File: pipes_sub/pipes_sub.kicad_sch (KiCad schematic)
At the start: 28 parts, among them J1 2x8 Header, J2 2x5 Header, J4 2x5 Header, U2 TL072CP

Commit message: Changes labels: VCO to SIG
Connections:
- net VCO renamed SIG
- net VCO1 renamed SIG1
- net VCO2 renamed SIG2
- net VCO3 renamed SIG3
- net VCO4 renamed SIG4
- net VCO5 renamed SIG5
- net VCO6 renamed SIG6
- net VCO7 renamed SIG7
- net VCO8 renamed SIG8
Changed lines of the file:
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@@
     )
   )
-  (global_label "VCO8" (shape input) (at 195.326 76.2 180) (fields_autoplaced)
+  (global_label "SIG8" (shape input) (at 195.326 76.2 180) (fields_autoplaced)
     (effects (font (size 1.27 1.27)) (justify right))
     (property "Intersheet References" "${INTERSHEET_REFS}" (id 0) (at 188.0143 76.1206 0)
@@
     )
   )
-  (global_label "VCO4" (shape input) (at 195.326 45.72 180) (fields_autoplaced)
+  (global_label "SIG4" (shape input) (at 195.326 45.72 180) (fields_autoplaced)
     (effects (font (size 1.27 1.27)) (justify right))
     (property "Intersheet References" "${INTERSHEET_REFS}" (id 0) (at 188.0143 45.6406 0)
@@
     )
   )
-  (global_label "VCO7" (shape input) (at 195.326 68.58 180) (fields_autoplaced)
+  (global_label "SIG7" (shape input) (at 195.326 68.58 180) (fields_autoplaced)
     (effects (font (size 1.27 1.27)) (justify right))
     (property "Intersheet References" "${INTERSHEET_REFS}" (id 0) (at 188.0143 68.5006 0)
@@
     )
   )
-  (global_label "VCO6" (shape input) (at 195.326 60.96 180) (fields_autoplaced)
+  (global_label "SIG6" (shape input) (at 195.326 60.96 180) (fields_autoplaced)
     (effects (font (size 1.27 1.27)) (justify right))
     (property "Intersheet References" "${INTERSHEET_REFS}" (id 0) (at 188.0143 60.8806 0)
@@
     )
   )
-  (global_label "VCO1" (shape input) (at 195.326 22.86 180) (fields_autoplaced)
+  (global_label "SIG1" (shape input) (at 195.326 22.86 180) (fields_autoplaced)
     (effects (font (size 1.27 1.27)) (justify right))
     (property "Intersheet References" "${INTERSHEET_REFS}" (id 0) (at 188.0143 22.7806 0)
@@
     )
   )
-  (global_label "VCO2" (shape input) (at 195.326 30.48 180) (fields_autoplaced)
+  (global_label "SIG2" (shape input) (at 195.326 30.48 180) (fields_autoplaced)
     (effects (font (size 1.27 1.27)) (justify right))
     (property "Intersheet References" "${INTERSHEET_REFS}" (id 0) (at 188.0143 30.4006 0)
@@
     )
   )
-  (global_label "VCO" (shape input) (at 111.125 52.07 180) (fields_autoplaced)
+  (global_label "SIG" (shape input) (at 111.125 52.07 180) (fields_autoplaced)
     (effects (font (size 1.27 1.27)) (justify right))
-    (property "Intersheet References" "${INTERSHEET_REFS}" (id 0) (at 105.0229 51.9906 0)
+    (property "Intersheet References" "${INTERSHEET_REFS}" (id 0) (at 105.6276 51.9906 0)
       (effects (font (size 1.27 1.27)) (justify right) hide)
     )
@@
     )
   )
-  (global_label "VCO3" (shape input) (at 195.326 38.1 180) (fields_autoplaced)
+  (global_label "SIG3" (shape input) (at 195.326 38.1 180) (fields_autoplaced)
     (effects (font (size 1.27 1.27)) (justify right))
     (property "Intersheet References" "${INTERSHEET_REFS}" (id 0) (at 188.0143 38.0206 0)
@@
     )
   )
-  (global_label "VCO5" (shape input) (at 195.326 53.34 180) (fields_autoplaced)
+  (global_label "SIG5" (shape input) (at 195.326 53.34 180) (fields_autoplaced)
     (effects (font (size 1.27 1.27)) (justify right))
     (property "Intersheet References" "${INTERSHEET_REFS}" (id 0) (at 188.0143 53.2606 0)
@@
     )
   )
-  (global_label "VCO" (shape output) (at 252.095 33.02 0) (fields_autoplaced)
+  (global_label "SIG" (shape output) (at 252.095 33.02 0) (fields_autoplaced)
     (effects (font (size 1.27 1.27)) (justify left))
-    (property "Intersheet References" "${INTERSHEET_REFS}" (id 0) (at 258.1971 32.9406 0)
+    (property "Intersheet References" "${INTERSHEET_REFS}" (id 0) (at 257.5924 32.9406 0)
       (effects (font (size 1.27 1.27)) (justify left) hide)
     )

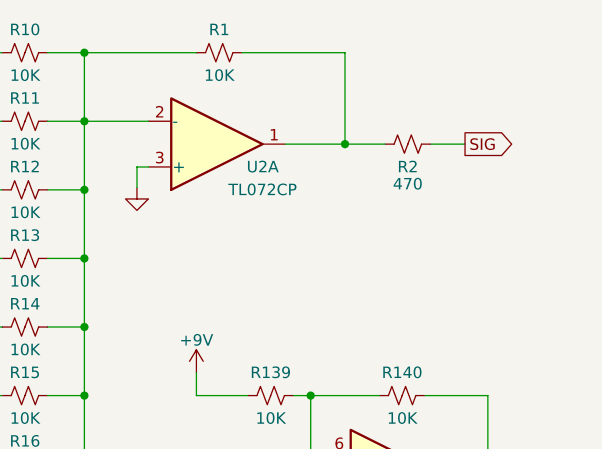
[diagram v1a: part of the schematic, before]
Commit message: Adds digikey bom merge. Uses local graphics for panel.
Adds bambooh graphics
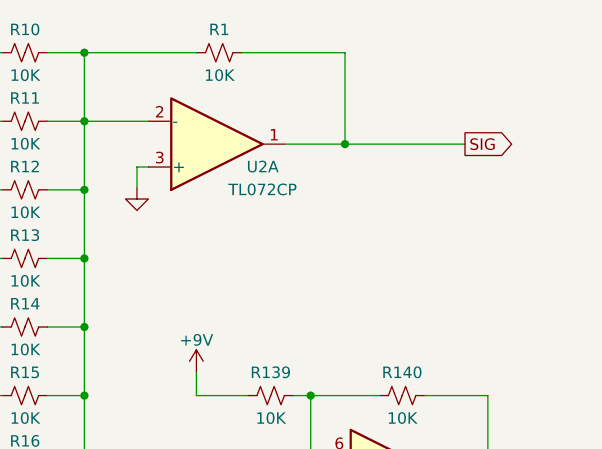
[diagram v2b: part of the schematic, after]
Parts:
- removed R2: 470, Resistor_SMD:R_0805_2012Metric_Pad1.20x1.40mm_HandSolder, symbol Device:R_Small_US
- J2: Digi-Key Part 732-5382-1-ND -> (none)
- J4: LCSC Part # C124391 -> (none)
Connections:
- net SIG: now also R1.1, U2.1

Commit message: Version 1.1 of boards
Changes to use NSL-32SR3 Vactrols
Fixes 3904 package
Adds 10-step waveform
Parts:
- TP1, TP2: LCSC Part # (none) -> C5199801
